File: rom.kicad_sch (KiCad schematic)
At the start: 5 parts, among them IC17 27C256, IC18 74LS08

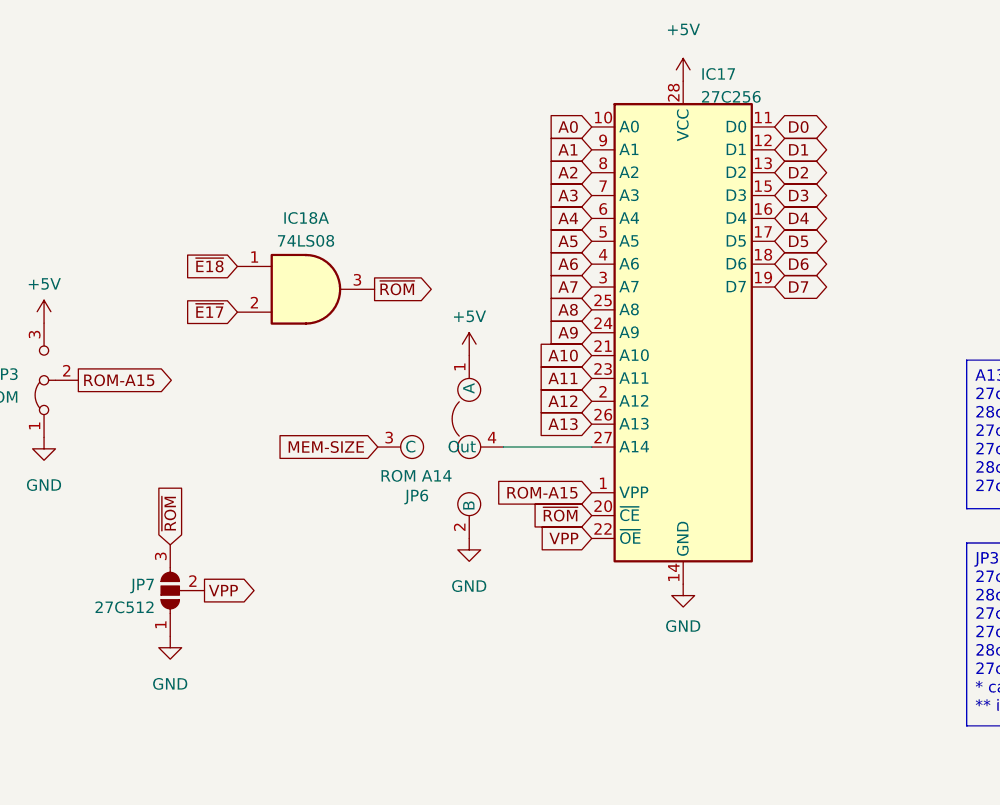
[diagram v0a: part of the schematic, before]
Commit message: update to keyboard switch option
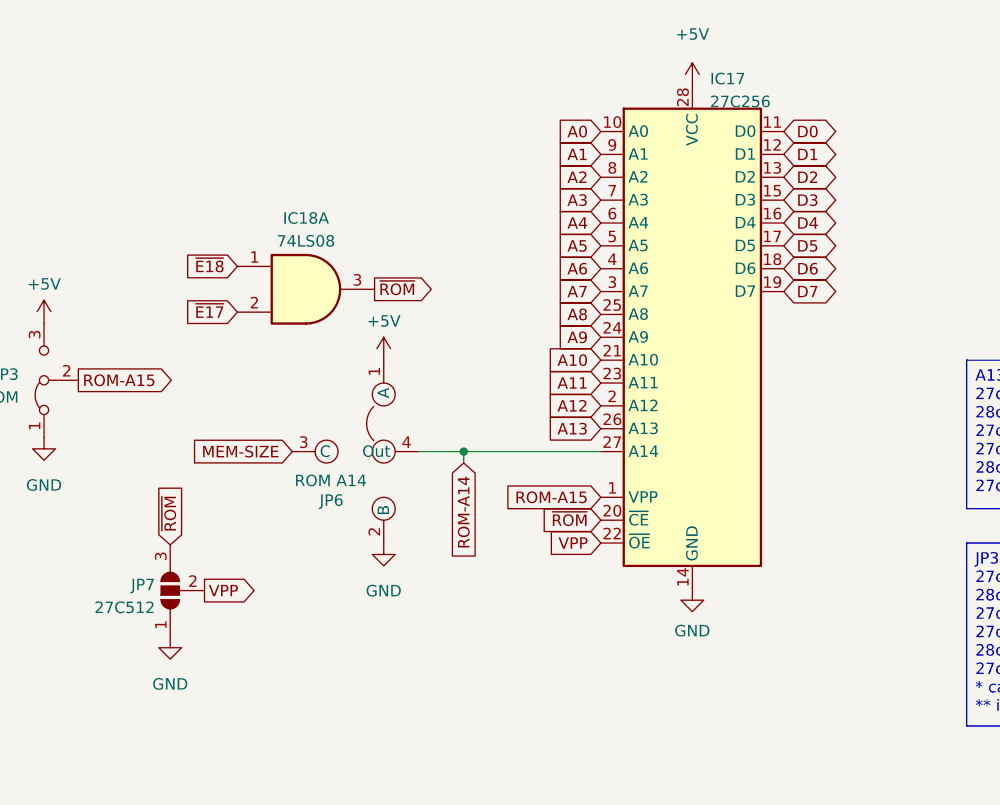
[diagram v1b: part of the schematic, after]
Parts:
- IC18: LCSC (none) -> C22394768
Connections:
- net ROM-A14: now reaches IC17.27 (A14), JP6.4 (Out)
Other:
- title: (none) -> Dragon CPU UK Revised
- moved on the sheet: IC17, JP6
